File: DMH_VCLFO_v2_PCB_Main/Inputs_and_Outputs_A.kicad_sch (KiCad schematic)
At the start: 41 parts, among them J1 TS_Jack_6.35mm_Sw, J19 Conn_01x08, J2 TS_Jack_6.35mm_Sw, J20 Conn_01x08, J21 IDA_02x05, J22 Conn_01x08, J23 Conn_01x08, J3 TS_Jack_6.35mm_Sw, J4 TS_Jack_6.35mm_Sw, J5 TS_Jack_6.35mm_Sw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

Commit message: Prepared for PCB design
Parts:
- J21: value IDA_02x05 -> IDC_02x05
- RV1, RV2: footprint SynthStuff:Potentiometer_TT_P110KH1 -> SynthStuff:Potentiometer_Alpha_RD901F-40-00D_Single_Vertical
- U1: footprint (none) -> Package_DIP:DIP-14_W7.62mm_Socket
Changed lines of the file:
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@@
 		(exclude_from_sim no)
 		(in_bom yes)
-		(on_board no)
+		(on_board yes)
 		(dnp no)
 		(fields_autoplaced yes)
@@
 		(exclude_from_sim no)
 		(in_bom yes)
-		(on_board no)
+		(on_board yes)
 		(dnp no)
 		(fields_autoplaced yes)
@@
 			)
 		)
-		(property "Footprint" ""
+		(property "Footprint" "Package_DIP:DIP-14_W7.62mm_Socket"
 			(at 166.37 29.21 0)
 			(effects
@@
 		(exclude_from_sim no)
 		(in_bom yes)
-		(on_board no)
+		(on_board yes)
 		(dnp no)
 		(property "Reference" "R7"
@@
 		(exclude_from_sim no)
 		(in_bom yes)
-		(on_board no)
+		(on_board yes)
 		(dnp no)
 		(fields_autoplaced yes)
@@
 		(exclude_from_sim no)
 		(in_bom yes)
-		(on_board no)
+		(on_board yes)
 		(dnp no)
 		(property "Reference" "R9"
@@
 		(exclude_from_sim no)
 		(in_bom yes)
-		(on_board no)
+		(on_board yes)
 		(dnp no)
 		(fields_autoplaced yes)
@@
 		(exclude_from_sim no)
 		(in_bom yes)
-		(on_board no)
+		(on_board yes)
 		(dnp no)
 		(property "Reference" "RV3"
@@
 		(exclude_from_sim no)
 		(in_bom yes)
-		(on_board no)
+		(on_board yes)
 		(dnp no)
 		(fields_autoplaced yes)
@@
 		(exclude_from_sim no)
 		(in_bom yes)
-		(on_board no)
+		(on_board yes)
 		(dnp no)
 		(property "Reference" "RV2"
@@
 			)
 		)
-		(property "Footprint" "SynthStuff:Potentiometer_TT_P110KH1"
+		(property "Footprint" "SynthStuff:Potentiometer_Alpha_RD901F-40-00D_Single_Vertical"
 			(at 25.4 76.2 0)
 			(effects
@@
 		(exclude_from_sim no)
 		(in_bom yes)
-		(on_board no)
+		(on_board yes)
 		(dnp no)
 		(property "Reference" "R17"
@@
 		(exclude_from_sim no)
 		(in_bom yes)
-		(on_board no)
+		(on_board yes)
 		(dnp no)
 		(fields_autoplaced yes)
@@
 		(exclude_from_sim no)
 		(in_bom yes)
-		(on_board no)
+		(on_board yes)
 		(dnp no)
 		(fields_autoplaced yes)
@@
 		(exclude_from_sim no)
 		(in_bom yes)
-		(on_board no)
+		(on_board yes)
 		(dnp no)
 		(property "Reference" "R3"
@@
 		(exclude_from_sim no)
 		(in_bom yes)
-		(on_board no)
+		(on_board yes)
 		(dnp no)
 		(fields_autoplaced yes)
@@
 		(exclude_from_sim no)
 		(in_bom yes)
-		(on_board no)
+		(on_board yes)
 		(dnp no)
 		(property "Reference" "R15"
@@
 			)
 		)
-		(property "Footprint" ""
+		(property "Footprint" "Package_DIP:DIP-14_W7.62mm_Socket"
 			(at 166.37 87.63 0)
 			(effects
@@
 		(exclude_from_sim no)
 		(in_bom yes)
-		(on_board no)
+		(on_board yes)
 		(dnp no)
 		(fields_autoplaced yes)
@@
 		(exclude_from_sim no)
 		(in_bom yes)
-		(on_board no)
+		(on_board yes)
 		(dnp no)
 		(fields_autoplaced yes)
@@
 		(exclude_from_sim no)
 		(in_bom yes)
-		(on_board no)
+		(on_board yes)
 		(dnp no)
 		(property "Reference" "#PWR013"
@@
 			)
 		)
-		(property "Value" "IDA_02x05"
+		(property "Value" "IDC_02x05"
 			(at 146.05 170.18 0)
 			(effects
@@
 		(exclude_from_sim no)
 		(in_bom yes)
-		(on_board no)
+		(on_board yes)
 		(dnp no)
 		(property "Reference" "R12"
@@
 		(exclude_from_sim no)
 		(in_bom yes)
-		(on_board no)
+		(on_board yes)
 		(dnp no)
 		(fields_autoplaced yes)
@@
 		(exclude_from_sim no)
 		(in_bom yes)
-		(on_board no)
+		(on_board yes)
 		(dnp no)
 		(fields_autoplaced yes)
@@
 		(exclude_from_sim no)
 		(in_bom yes)
-		(on_board no)
+		(on_board yes)
 		(dnp no)
 		(property "Reference" "R11"
@@
 		(exclude_from_sim no)
 		(in_bom yes)
-		(on_board no)
+		(on_board yes)
 		(dnp no)
 		(fields_autoplaced yes)
@@
 		(exclude_from_sim no)
 		(in_bom yes)
-		(on_board no)
+		(on_board yes)
 		(dnp no)
 		(fields_autoplaced yes)
@@
 		(exclude_from_sim no)
 		(in_bom yes)
-		(on_board no)
+		(on_board yes)
 		(dnp no)
 		(fields_autoplaced yes)
@@
 		(exclude_from_sim no)
 		(in_bom yes)
-		(on_board no)
+		(on_board yes)
 		(dnp no)
 		(fields_autoplaced yes)
@@
 		(exclude_from_sim no)
 		(in_bom yes)
-		(on_board no)
+		(on_board yes)
 		(dnp no)
 		(fields_autoplaced yes)
@@
 		(exclude_from_sim no)
 		(in_bom yes)
-		(on_board no)
+		(on_board yes)
 		(dnp no)
 		(property "Reference" "RV4"
@@
 		(exclude_from_sim no)
 		(in_bom yes)
-		(on_board no)
+		(on_board yes)
 		(dnp no)
 		(fields_autoplaced yes)
@@
 		(exclude_from_sim no)
 		(in_bom yes)
-		(on_board no)
+		(on_board yes)
 		(dnp no)
 		(property "Reference" "RV1"
@@
 			)
 		)
-		(property "Footprint" "SynthStuff:Potentiometer_TT_P110KH1"
+		(property "Footprint" "SynthStuff:Potentiometer_Alpha_RD901F-40-00D_Single_Vertical"
 			(at 63.5 69.85 0)
 			(effects
@@
 		(exclude_from_sim no)
 		(in_bom yes)
-		(on_board no)
+		(on_board yes)
 		(dnp no)
 		(fields_autoplaced yes)
@@
 			)
 		)
-		(property "Footprint" ""
+		(property "Footprint" "Package_DIP:DIP-14_W7.62mm_Socket"
 			(at 168.91 54.61 0)
 			(effects

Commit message: Main PCB comp placement in progress
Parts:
- J19, J20: footprint Connector_PinHeader_2.54mm:PinHeader_1x08_P2.54mm_Vertical -> Connector_PinSocket_2.54mm:PinSocket_1x08_P2.54mm_Vertical
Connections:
- net A_BusCV_Sw_p2_C: now also J20.4 (Pin_4); no longer J20.7 (Pin_7)
- net A_BusCV_Sw_p2_M: now also J23.4 (Pin_4); no longer J23.7 (Pin_7)
- net A_CV_Amt_Pot_p2_C: now also J19.6 (Pin_6); no longer J19.4 (Pin_4)
- net A_CV_Amt_Pot_p2_M: now also J22.6 (Pin_6); no longer J22.4 (Pin_4)
- net A_FRng_Trim_p2_C: now also J19.1 (Pin_1); no longer J19.6 (Pin_6)
- net A_FRng_Trim_p2_M: now also J22.1 (Pin_1); no longer J22.6 (Pin_6)
- net A_Freq_Pot_p2_C: now also J19.4 (Pin_4); no longer J19.3 (Pin_3)
- net A_Freq_Pot_p2_M: now also J22.4 (Pin_4); no longer J22.3 (Pin_3)
- net A_Rmp_C: now also SW3.3 (C); no longer SW3.1 (A)
- net A_Rnd_C: now also SW3.1 (A); no longer SW3.3 (C)
- net A_Rng_Sw_p1_C: now also J19.3 (Pin_3); no longer J19.1 (Pin_1)
- net A_Rng_Sw_p1_M: now also J22.3 (Pin_3); no longer J22.1 (Pin_1)
- net A_Sin_C: now also J20.6 (Pin_6), SW4.3 (C); no longer J20.4 (Pin_4), SW4.1 (A)
- net A_Sin_M: now also J23.6 (Pin_6); no longer J23.4 (Pin_4)
- net A_Sin_Tri_Sw_p2_C: now also J20.7 (Pin_7); no longer J20.5 (Pin_5)
- net A_Sin_Tri_Sw_p2_M: now also J23.7 (Pin_7); no longer J23.5 (Pin_5)
- net A_Tri_C: now also J20.8 (Pin_8), SW4.1 (A); no longer J20.6 (Pin_6), SW4.3 (C)
- net A_Tri_M: now also J23.8 (Pin_8); no longer J23.6 (Pin_6)
- net A_VOct_Trim_p12_C: now also J19.8 (Pin_8); no longer J19.7 (Pin_7)
- net A_VOct_Trim_p12_M: now also J22.8 (Pin_8); no longer J22.7 (Pin_7)
- net A_VOct_Trim_p3_C: now also J19.7 (Pin_7); no longer J19.8 (Pin_8)
- net A_VOct_Trim_p3_M: now also J22.7 (Pin_7); no longer J22.8 (Pin_8)
- net Bus_CV_C: now also J20.5 (Pin_5), SW1.1 (A); no longer J20.8 (Pin_8), SW1.3 (C)
- net Bus_CV_M: now also J23.5 (Pin_5); no longer J23.8 (Pin_8)
- net GND: no longer J21.10 (Pin_10), J21.4 (Pin_4), J21.5 (Pin_5), J21.9 (Pin_9)
- net A_Sync_TN_M: now reaches J21.1 (Pin_1)
- net A_Sync_TN_M: now also J2.TN
- net Out A Rmp/Rnd TN: no longer names the net of J21.6 (Pin_6)
- net Out A Rmp/Rnd TN: no longer J5.TN
- net Out A Saw TN: no longer names the net of J4.TN
- net Out A Saw TN: no longer J21.3 (Pin_3)
- net Out A Sin/Tri TN: no longer names the net of J21.7 (Pin_7)
- net Out A Sin/Tri TN: no longer J6.TN
- net Out A Sqr TN: no longer names the net of J21.8 (Pin_8)
- net Out A Sqr TN: no longer J3.TN
- net Sync A TN renamed A_Out_Sqr_TN_M
- net A_Out_Sqr_TN_M: now also J3.TN; no longer J2.TN
- new net A_Out_Sin_Tri_TN_M: J21.3 (Pin_3), J6.TN
- no-connect marks 2 -> 3

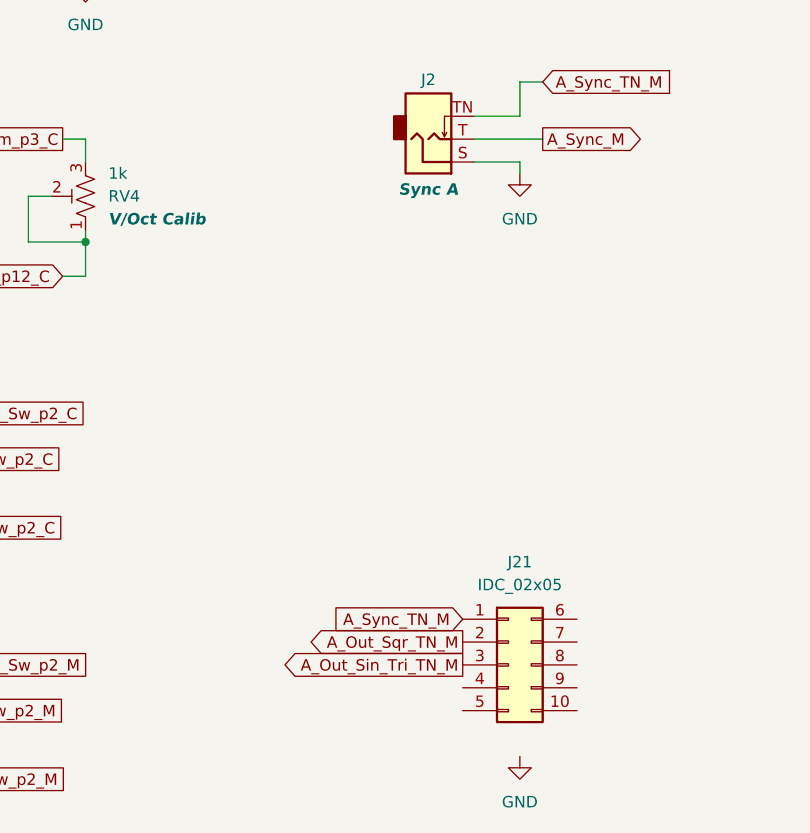
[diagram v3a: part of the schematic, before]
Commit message: Main PCB placement done
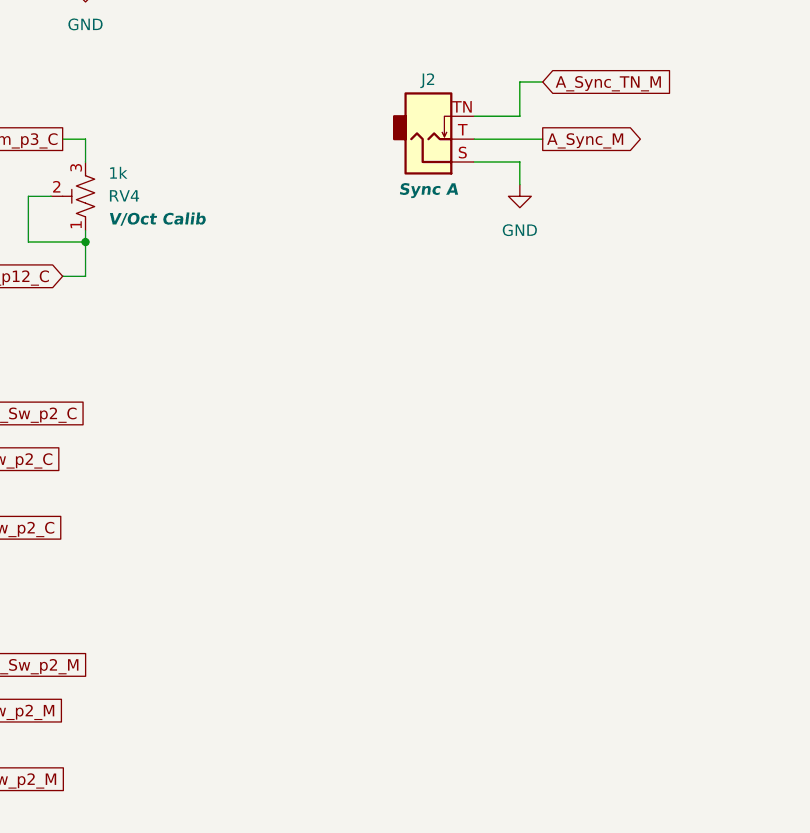
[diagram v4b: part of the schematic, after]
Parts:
- removed J21: IDC_02x05, SynthStuff:IDC-Header_2x05_P2.54mm_Vertical_BackBone, symbol SynthStuff:BackBone_Connector_10Pin
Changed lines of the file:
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@@
 	(wire
 		(pts
-			(xy 146.05 124.46) (xy 146.05 123.19)
+			(xy 146.05 125.73) (xy 146.05 123.19)
 		)
 		(stroke
@@
 		)
 	)
-	(global_label "A_Out_Sin_Tri_TN_M"
-		(shape output)
-		(at 139.7 179.07 180)
-		(fields_autoplaced yes)
-		(effects
-			(font
-				(size 1.27 1.27)
-			)
-			(justify right)
-		)
-		(property "Intersheetrefs" "${INTERSHEET_REFS}"
-			(at 118.5116 179.07 0)
-			(effects
-				(font
-					(size 1.27 1.27)
-				)
-				(justify right)
-				(hide yes)
-			)
-		)
-	)
 	(global_label "A_Tri_C"
 		(shape input)
@@
 		)
 	)
-	(global_label "A_Sync_TN_M"
-		(shape input)
-		(at 139.7 173.99 180)
-		(fields_autoplaced yes)
-		(effects
-			(font
-				(size 1.27 1.27)
-			)
-			(justify right)
-		)
-		(property "Intersheetrefs" "${INTERSHEET_REFS}"
-			(at 124.5592 173.99 0)
-			(effects
-				(font
-					(size 1.27 1.27)
-				)
-				(justify right)
-				(hide yes)
-			)
-		)
-	)
 	(global_label "A_Rng_Sw_p1_M"
 		(shape passive)
@@
 		)
 	)
-	(global_label "A_Out_Sqr_TN_M"
-		(shape output)
-		(at 139.7 176.53 180)
-		(fields_autoplaced yes)
-		(effects
-			(font
-				(size 1.27 1.27)
-			)
-			(justify right)
-		)
-		(property "Intersheetrefs" "${INTERSHEET_REFS}"
-			(at 121.6564 176.53 0)
-			(effects
-				(font
-					(size 1.27 1.27)
-				)
-				(justify right)
-				(hide yes)
-			)
-		)
-	)
 	(global_label "A_Rnd_C"
 		(shape passive)
@@
 	)
 	(symbol
-		(lib_id "power:GND")
-		(at 146.05 189.23 0)
-		(unit 1)
-		(exclude_from_sim no)
-		(in_bom yes)
-		(on_board yes)
-		(dnp no)
-		(fields_autoplaced yes)
-		(property "Reference" "#PWR018"
-			(at 146.05 195.58 0)
-			(effects
-				(font
-					(size 1.27 1.27)
-				)
-				(hide yes)
-			)
-		)
-		(property "Value" "GND"
-			(at 146.05 194.31 0)
-			(effects
-				(font
-					(size 1.27 1.27)
-				)
-			)
-		)
-		(property "Footprint" ""
-			(at 146.05 189.23 0)
-			(effects
-				(font
-					(size 1.27 1.27)
-				)
-				(hide yes)
-			)
-		)
-		(property "Datasheet" ""
-			(at 146.05 189.23 0)
-			(effects
-				(font
-					(size 1.27 1.27)
-				)
-				(hide yes)
-			)
-		)
-		(property "Description" "Power symbol creates a global label with name \"GND\" , ground"
-			(at 146.05 189.23 0)
-			(effects
-				(font
-					(size 1.27 1.27)
-				)
-				(hide yes)
-			)
-		)
-		(pin "1"
-		)
-		(instances
-			(project "DMH_VCLFO_v2_PCB_Main"
-				(path "/58f4306d-5387-4983-bb08-41a2313fd315/ce3fef8b-9f1d-4178-b50b-4a046c030679"
-					(reference "#PWR018")
-					(unit 1)
-				)
-			)
-		)
-	)
-	(symbol
 		(lib_id "Device:R_US")
 		(at 38.1 105.41 90)
@@
 	)
 	(symbol
-		(lib_id "SynthStuff:BackBone_Connector_10Pin")
-		(at 146.05 179.07 0)
-		(unit 1)
-		(exclude_from_sim no)
-		(in_bom yes)
-		(on_board yes)
-		(dnp no)
-		(fields_autoplaced yes)
-		(property "Reference" "J21"
-			(at 146.05 167.64 0)
-			(effects
-				(font
-					(size 1.27 1.27)
-				)
-			)
-		)
-		(property "Value" "IDC_02x05"
-			(at 146.05 170.18 0)
-			(effects
-				(font
-					(size 1.27 1.27)
-				)
-			)
-		)
-		(property "Footprint" "SynthStuff:IDC-Header_2x05_P2.54mm_Vertical_BackBone"
-			(at 144.78 181.61 0)
-			(effects
-				(font
-					(size 1.27 1.27)
-				)
-				(hide yes)
-			)
-		)
-		(property "Datasheet" "~"
-			(at 144.78 181.61 0)
-			(effects
-				(font
-					(size 1.27 1.27)
-				)
-				(hide yes)
-			)
-		)
-		(property "Description" "IDC jack, 2x5 pins, row a carries same signals as row b."
-			(at 144.78 181.61 0)
-			(effects
-				(font
-					(size 1.27 1.27)
-				)
-				(hide yes)
-			)
-		)
-		(property "Function" ""
-			(at 146.05 179.07 0)
-			(effects
-				(font
-					(size 1.27 1.27)
-				)
-			)
-		)
-		(pin "1"
-		)
-		(pin "2"
-		)
-		(pin "3"
-		)
-		(pin "8"
-		)
-		(pin "5"
-		)
-		(pin "10"
-		)
-		(pin "4"
-		)
-		(pin "6"
-		)
-		(pin "7"
-		)
-		(pin "9"
-		)
-		(instances
-			(project "DMH_VCLFO_v2_PCB_Main"
-				(path "/58f4306d-5387-4983-bb08-41a2313fd315/ce3fef8b-9f1d-4178-b50b-4a046c030679"
-					(reference "J21")
-					(unit 1)
-				)
-			)
-		)
-	)
-	(symbol
 		(lib_id "Device:R_US")
 		(at 97.79 97.79 180)
@@
 	(symbol
 		(lib_id "power:GND")
-		(at 146.05 124.46 0)
+		(at 146.05 125.73 0)
 		(unit 1)
 		(exclude_from_sim no)
@@
 		(fields_autoplaced yes)
 		(property "Reference" "#PWR014"
-			(at 146.05 130.81 0)
+			(at 146.05 132.08 0)
 			(effects
 				(font
@@
 		)
 		(property "Value" "GND"
-			(at 146.05 129.54 0)
+			(at 146.05 130.81 0)
 			(effects
 				(font
@@
 		)
 		(property "Footprint" ""
-			(at 146.05 124.46 0)
+			(at 146.05 125.73 0)
 			(effects
 				(font
@@
 		)
 		(property "Datasheet" ""
-			(at 146.05 124.46 0)
+			(at 146.05 125.73 0)
 			(effects
 				(font
@@
 		)
 		(property "Description" "Power symbol creates a global label with name \"GND\" , ground"
-			(at 146.05 124.46 0)
+			(at 146.05 125.73 0)
 			(effects
 				(font

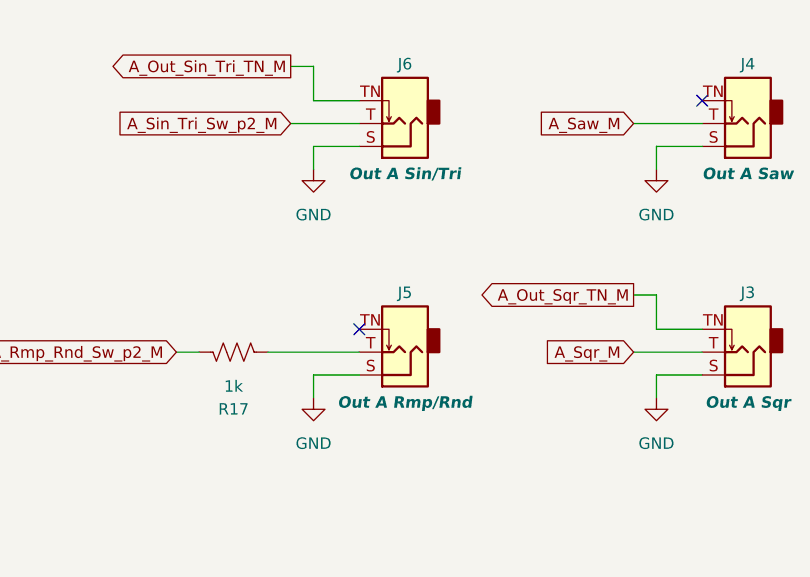
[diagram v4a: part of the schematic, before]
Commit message: Main PCB routing done
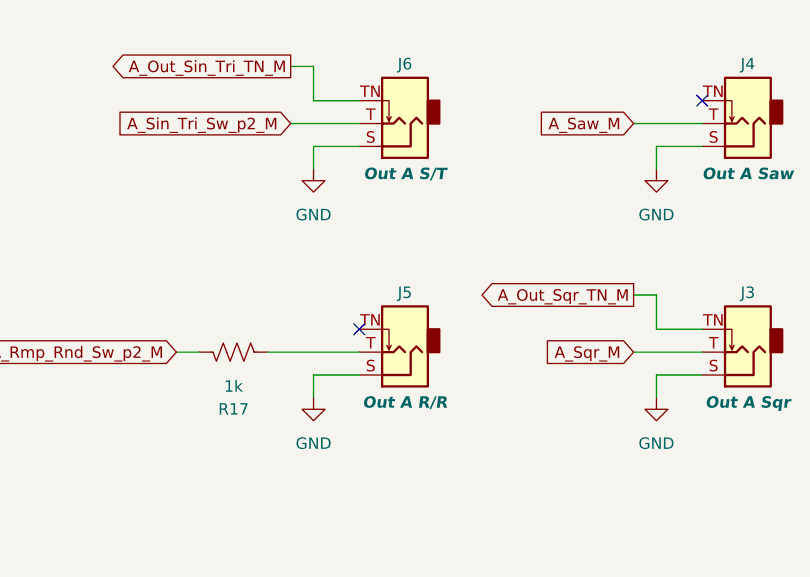
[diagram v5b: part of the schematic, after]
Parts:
- J5: Function Out A Rmp/Rnd -> Out A R/R
- J6: Function Out A Sin/Tri -> Out A S/T
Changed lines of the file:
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@@
 			)
 		)
-		(property "Function" "Out A Sin/Tri"
+		(property "Function" "Out A S/T"
 			(at 228.6 119.888 0)
 			(effects
@@
 			)
 		)
-		(property "Function" "Out A Rmp/Rnd"
+		(property "Function" "Out A R/R"
 			(at 228.6 145.288 0)
 			(effects

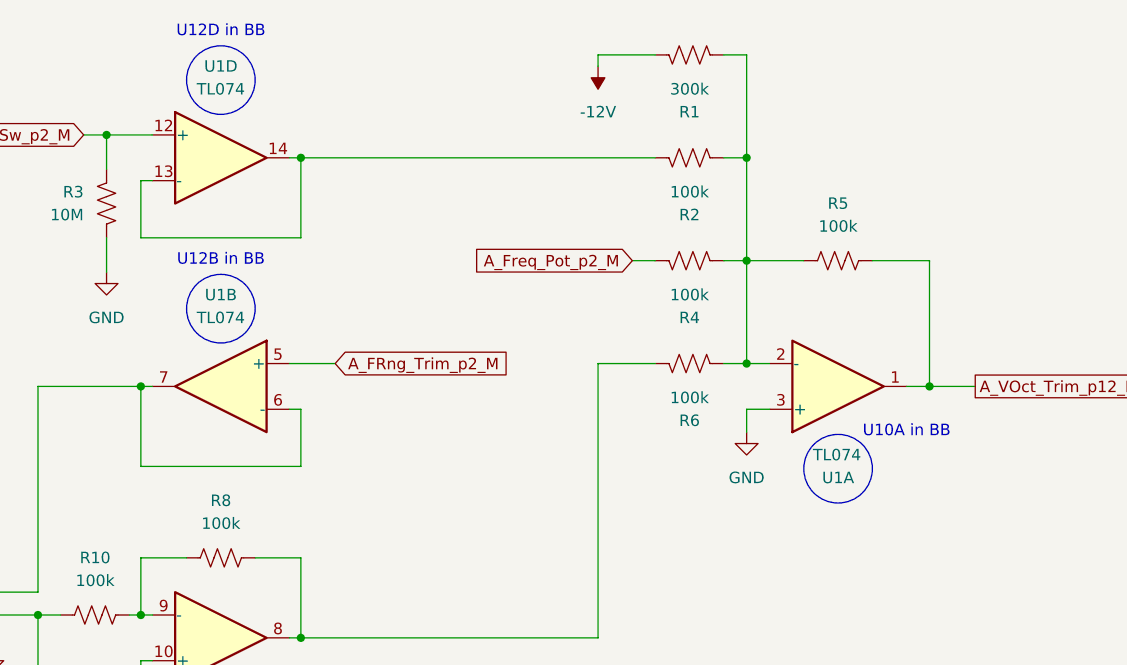
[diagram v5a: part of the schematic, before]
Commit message: Added project with Single VCLFO schematic
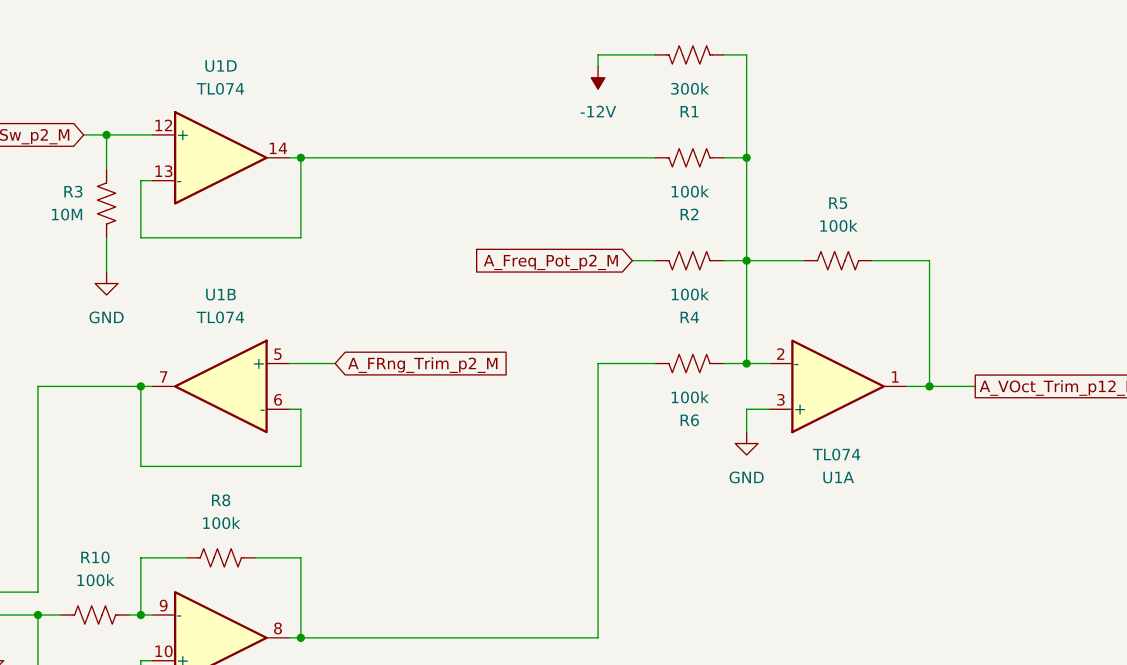
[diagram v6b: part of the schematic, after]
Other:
- note removed: "U10A in BB"
- note removed: "U12B in BB"
- note removed: "U12D in BB"
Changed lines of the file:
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@@
 		(comment 1 "PCB for 10cm Kosmo format synthesizer module")
-	)
-	(circle
-		(center 236.22 66.294)
-		(radius 3.81)
-		(stroke
-			(width 0)
-			(type default)
-		)
-		(fill
-			(type none)
-		)
-	)
-	(circle
-		(center 167.64 48.514)
-		(radius 3.81)
-		(stroke
-			(width 0)
-			(type default)
-		)
-		(fill
-			(type none)
-		)
-	)
-	(circle
-		(center 167.64 23.114)
-		(radius 3.81)
-		(stroke
-			(width 0)
-			(type default)
-		)
-		(fill
-			(type none)
-		)
-	)
-	(text "U12B in BB"
-		(exclude_from_sim no)
-		(at 167.64 43.18 0)
-		(effects
-			(font
-				(size 1.27 1.27)
-			)
-		)
-	)
-	(text "U10A in BB"
-		(exclude_from_sim no)
-		(at 243.84 62.23 0)
-		(effects
-			(font
-				(size 1.27 1.27)
-			)
-		)
-	)
-	(text "U12D in BB"
-		(exclude_from_sim no)
-		(at 167.64 17.78 0)
-		(effects
-			(font
-				(size 1.27 1.27)
-			)
-		)
 	)
 	(junction
